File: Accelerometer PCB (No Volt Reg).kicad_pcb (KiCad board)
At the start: 2 copper layers, 77 x 55 mm, 21 parts, among them J1 S2B-PH-SM4-TB_LF__SN_, J2 M20-8770442, J3 MolexMicroSD, SW1 SW_Push, SW2 SW_Push, U1 Swan v3.0, U2 Sysrox Accelerometer, U3 Adafruit DS3231 RTC

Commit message: Add files via upload
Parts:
- moved R2 0.70 mm to (105.0, 106.7)
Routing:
- net Net-(J2-VCC): track 199.9 -> 200.6 mm
- net GND: vias 0 -> 24

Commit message: Add files via upload
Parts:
- renumbered C2 to C1, C3 to C2, C4 to C3, C5 to C4, C6 to C5, C7 to C6

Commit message: Add files via upload
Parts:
- J1: value S2B-PH-SM4-TB_LF__SN_ -> Power Connector
- R1, R2: value 100k -> 100kΩ
- moved U2 19.8 mm to (170.9, 82.1), turned to 0 degrees
- moved D1 14.3 mm to (126.0, 80.9)
- moved C3 13.6 mm to (130.6, 85.0)
- moved C1 12.9 mm to (131.0, 77.9), turned to 90 degrees
- moved C6 12.8 mm to (130.0, 88.0)
- moved J3 12.8 mm to (124.2, 98.6)
- moved H2 12.6 mm to (119.0, 119.0)
- moved H1 12.2 mm to (119.0, 73.0)
- moved J1 12.1 mm to (122.1, 83.3)
- moved SW1 11.8 mm to (128.7, 111.1), turned to 180 degrees
- moved SW2 11.7 mm to (128.7, 119.3), turned to 180 degrees
- moved C2 11.6 mm to (179.3, 73.9)
- moved H4 11.4 mm to (185.0, 119.0)
- moved H3 11.2 mm to (185.0, 73.0)
- moved U1 11.1 mm to (128.2, 64.5)
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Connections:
- net Net-(D1-K) renamed Input Power
- net Net-(J2-SCL) renamed /OLED Serial Clock
- net Net-(J2-SDA) renamed /OLED Serial Data
- net Net-(J3-CD/DAT3) renamed /MicroSD Card Detect
- net Net-(J3-CLK) renamed /MicroSD Clock Line
- net Net-(J3-CMD) renamed /MicroSD MOSI
- net Net-(J3-DA0) renamed /MicroSD MISO
- net Net-(U1-A1) renamed /Switch 1 I/O
- net Net-(U1-A2) renamed /Switch 2 I/O
- net Net-(U1-D10) renamed /IMU Chip Select
- net Net-(U1-D11) renamed /IMU MOSI
- net Net-(U1-D12) renamed /IMU MISO
- net Net-(U1-D13) renamed /IMU Serial Clock
- net Net-(U1-D6) renamed /IMU Interrupt
- net Net-(U1-D8) renamed /RTC Square Wave
- net Net-(U1-SCL) renamed /RTC Clock Line
- net Net-(U1-SDA) renamed /RTC Data Line
- net Net-(U2-FSY) renamed /32kHz Frame Sync
- C2 pad 2: Net-(J2-VCC) -> +3.3V
- C3 pad 1: Net-(J2-VCC) -> +3.3V
- C4 pad 1: Net-(J2-VCC) -> +3.3V
- C5 pad 1: Net-(J2-VCC) -> +3.3V
- C6 pad 2: Net-(J2-VCC) -> +3.3V
- J2 pad 3: Net-(J2-VCC) -> +3.3V
- J3 pad 4: Net-(J2-VCC) -> +3.3V
- R1 pad 1: Net-(J3-DAT2) -> +3.3V
- R1 pad 2: Net-(J2-VCC) -> Net-(J3-DAT2)
- R2 pad 2: Net-(J2-VCC) -> +3.3V
- U1 pad 2: Net-(J2-VCC) -> +3.3V
- U2 pad 1: Net-(J2-VCC) -> +3.3V
- U3 pad 1: Net-(J2-VCC) -> +3.3V
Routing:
- net Net-(J2-VCC): track 200.6 -> 0.00 mm, vias 8 -> 0
- net +3.3V: track 0.00 -> 187.4 mm, vias 0 -> 8
- net /Switch 1 I/O: track 35.8 -> 22.3 mm, vias 2 -> 0
- net /Switch 2 I/O: track 40.2 -> 28.8 mm, vias 2 -> 0
- net Net-(D1-A): track 9.21 -> 3.95 mm
- net /RTC Data Line: track 27.4 -> 22.3 mm
- net Input Power: track 16.8 -> 12.2 mm
- net /IMU MISO: track 22.5 -> 19.6 mm
- net /IMU Chip Select: track 35.8 -> 33.1 mm
- net /IMU Serial Clock: track 23.1 -> 20.8 mm
- net Net-(J3-DAT2): track 13.0 -> 10.9 mm
- net /32kHz Frame Sync: track 28.3 -> 26.5 mm
- net /OLED Serial Data: track 20.5 -> 18.7 mm
- net /MicroSD Clock Line: track 27.6 -> 26.0 mm
- net /MicroSD MOSI: track 27.0 -> 25.4 mm
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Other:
- board size 77 x 55 mm -> 76 x 56 mm
- board text added: "Swan v3.0"
- board text removed: "MicroSD"
- board text removed: "PWR Conn"
- board text removed: "Swan"
- board text removed: "Sysrox IMU"

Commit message: Updated Project Files
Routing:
- net /MicroSD Card Detect: vias 4 -> 2

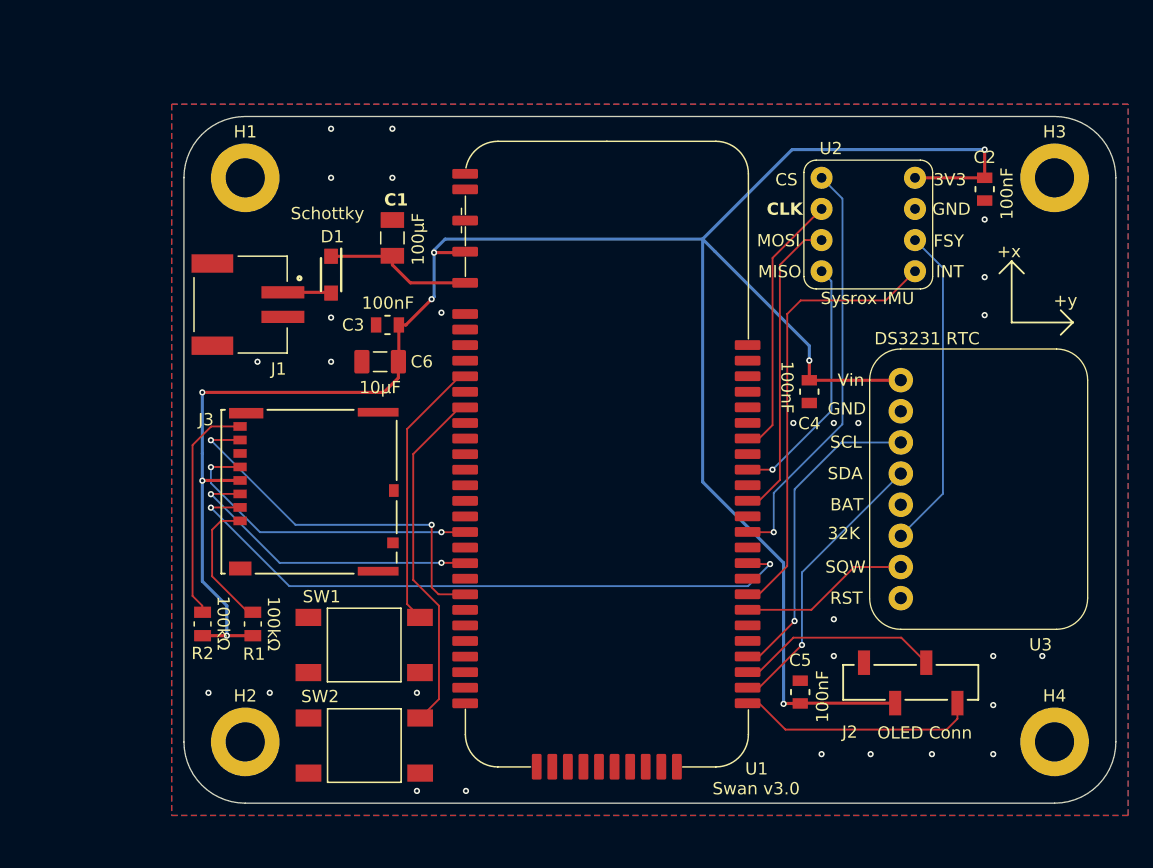
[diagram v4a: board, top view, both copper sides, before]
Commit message: Updated Screw Hole Connections and Labels
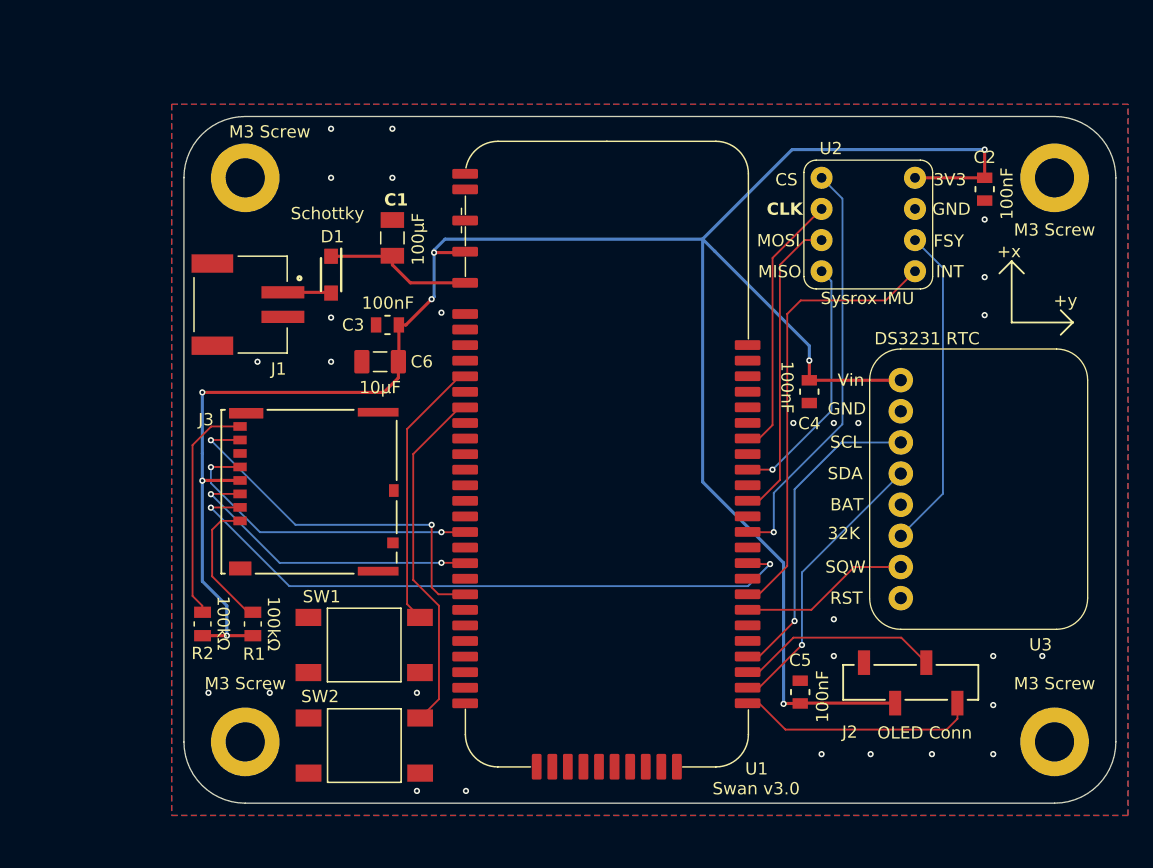
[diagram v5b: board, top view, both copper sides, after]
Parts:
- M3 Screw: renamed from H4
- M3 Screw: renamed from H1
- M3 Screw: renamed from H3
- M3 Screw: renamed from H2
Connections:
- M3 Screw pad 1: GND -> unconnected-(H4-Pad1)
- M3 Screw pad 1: GND -> unconnected-(H1-Pad1)
- M3 Screw pad 1: GND -> unconnected-(H3-Pad1)
- M3 Screw pad 1: GND -> unconnected-(H2-Pad1)
